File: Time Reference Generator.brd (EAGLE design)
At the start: 46.7 x 45.7 mm, 10 parts, among them IC1 4060N, IC2 4013N, X1 CRYSTAL_TINY

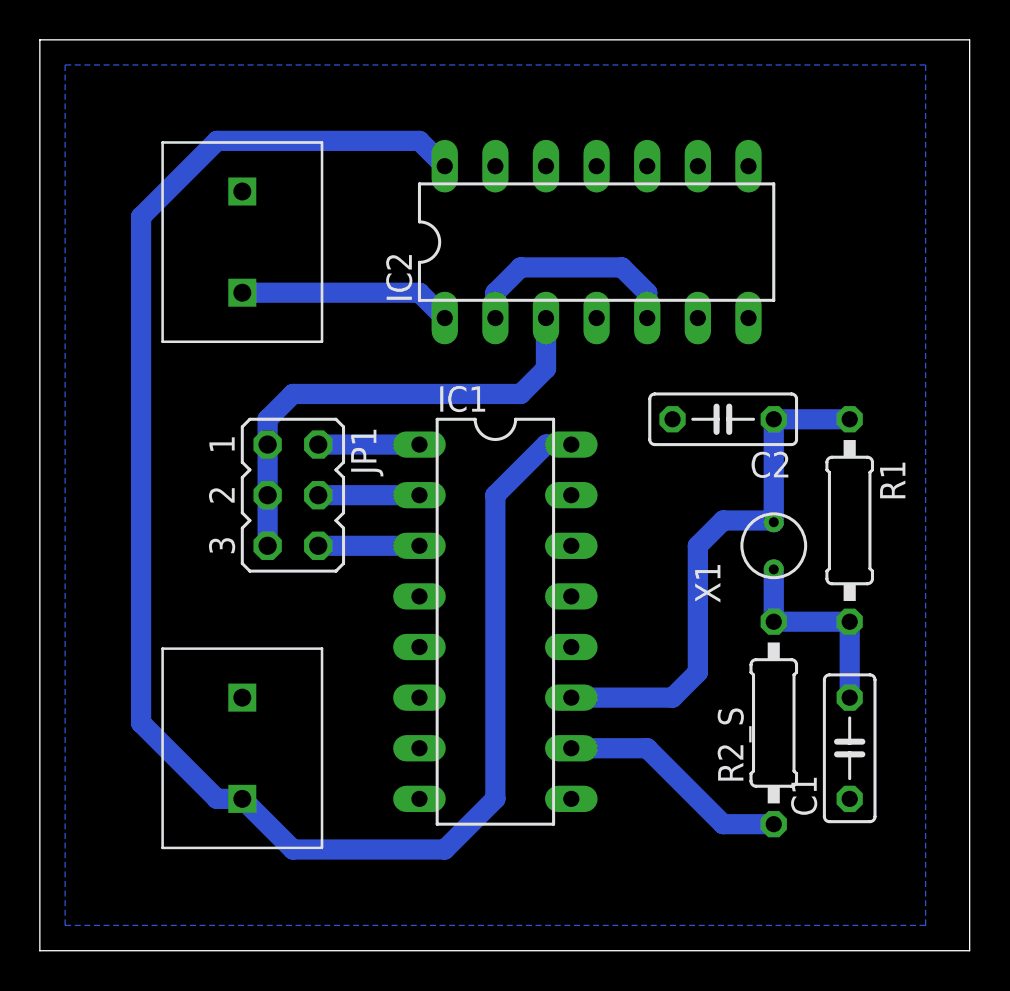
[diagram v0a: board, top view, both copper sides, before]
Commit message: Ajouter des capa de decouplage + augmentation isolation des thermals
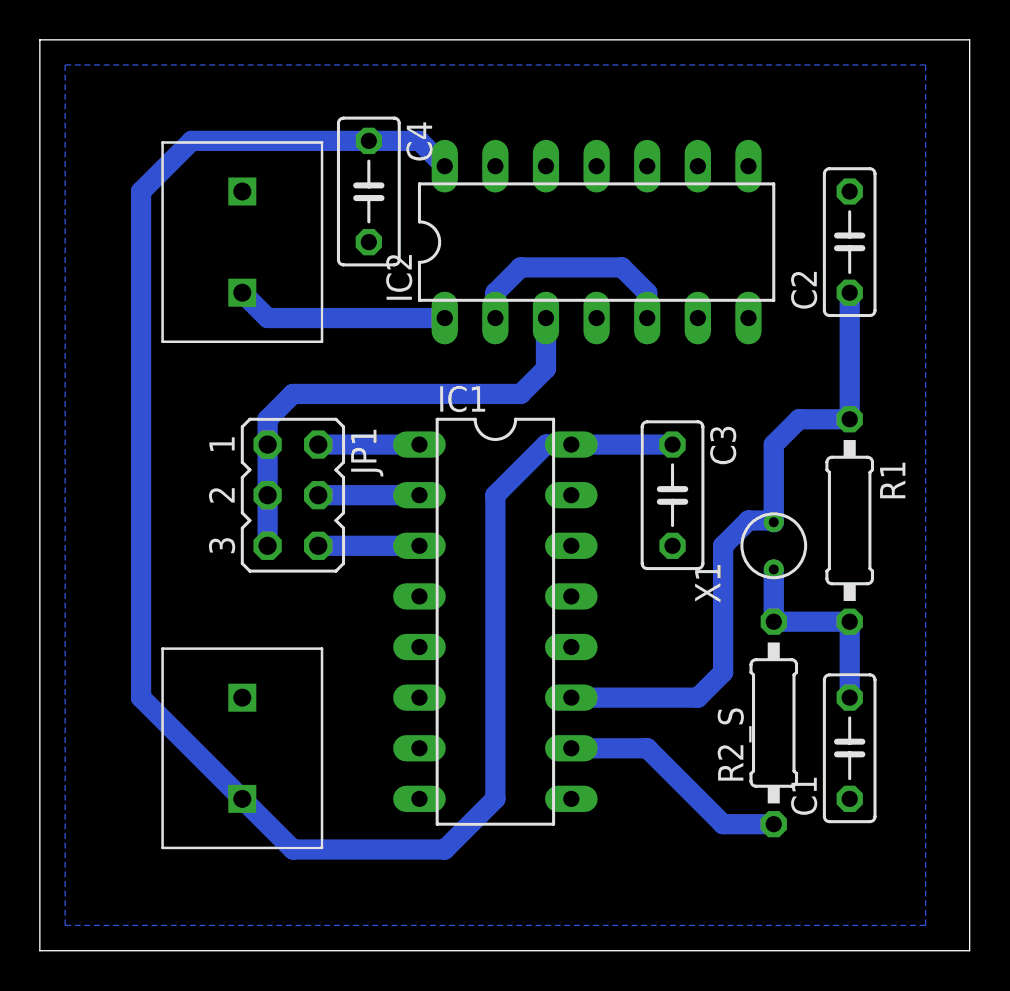
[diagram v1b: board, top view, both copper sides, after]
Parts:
- added C3, C4: 100n, resistor:C050-030X075
- moved C2 10.9 mm to (40.6, 35.6), turned to 90 degrees
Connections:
- net GND: now also C3.2, C4.2
- net VDD: now also C3.1, C4.1
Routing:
- net N$1: track 26.6 -> 32.2 mm
- net VDD: track 84.3 -> 89.4 mm
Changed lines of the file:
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@@
 <param name="srMinRoundness" value="0mil"/>
 <param name="srMaxRoundness" value="0mil"/>
-<param name="slThermalIsolate" value="10mil"/>
+<param name="slThermalIsolate" value="25mil"/>
 <param name="slThermalsForVias" value="0"/>
 <param name="dpMaxLengthDifference" value="10mm"/>
@@
 <element name="R1" library="resistor" package="0207/10" value="10M" x="40.64" y="21.59" rot="R270"/>
 <element name="C1" library="resistor" package="C050-025X075" value="25p" x="40.64" y="10.16" rot="R90"/>
-<element name="C2" library="resistor" package="C050-025X075" value="25p" x="34.29" y="26.67" rot="R180"/>
+<element name="C2" library="resistor" package="C050-025X075" value="25p" x="40.64" y="35.56" rot="R90"/>
 <element name="IC2" library="40xx" package="DIL14" value="4013N" x="27.94" y="35.56"/>
 <element name="POWER_SUPPY" library="PGT" package="SIL_2_0.2INCH" value="CON_2_SIL" x="10.16" y="10.16" rot="R180"/>
@@
 <element name="JP1" library="jumper" package="JP3Q" value="FREQ_SELECT" x="12.7" y="22.86" rot="R270"/>
 <element name="X1" library="PGT" package="WATCH-3X8-SPACED" value="CRYSTAL_TINY" x="36.83" y="20.32" rot="R90"/>
+<element name="C3" library="resistor" package="C050-030X075" value="100n" x="31.75" y="22.86" rot="R270"/>
+<element name="C4" library="resistor" package="C050-030X075" value="100n" x="16.51" y="38.1" rot="R270"/>
 </elements>
 <signals>
@@
 <wire x1="22.86" y1="22.86" x2="25.4" y2="25.4" width="1.016" layer="16"/>
 <wire x1="25.4" y1="25.4" x2="26.67" y2="25.4" width="1.016" layer="16"/>
-<wire x1="20.32" y1="39.37" x2="19.05" y2="40.64" width="1.016" layer="16"/>
-<wire x1="19.05" y1="40.64" x2="8.89" y2="40.64" width="1.016" layer="16"/>
-<wire x1="8.89" y1="40.64" x2="5.08" y2="36.83" width="1.016" layer="16"/>
-<wire x1="5.08" y1="36.83" x2="5.08" y2="11.43" width="1.016" layer="16"/>
-<wire x1="5.08" y1="11.43" x2="8.89" y2="7.62" width="1.016" layer="16"/>
-<wire x1="8.89" y1="7.62" x2="10.16" y2="7.62" width="1.016" layer="16"/>
+<contactref element="C3" pad="1"/>
+<contactref element="C4" pad="1"/>
+<wire x1="26.67" y1="25.4" x2="31.75" y2="25.4" width="1.016" layer="16"/>
+<wire x1="16.51" y1="40.64" x2="7.62" y2="40.64" width="1.016" layer="16"/>
+<wire x1="7.62" y1="40.64" x2="5.08" y2="38.1" width="1.016" layer="16"/>
+<wire x1="5.08" y1="38.1" x2="5.08" y2="12.7" width="1.016" layer="16"/>
+<wire x1="5.08" y1="12.7" x2="10.16" y2="7.62" width="1.016" layer="16"/>
+<wire x1="16.51" y1="40.64" x2="19.05" y2="40.64" width="1.016" layer="16"/>
+<wire x1="19.05" y1="40.64" x2="20.32" y2="39.37" width="1.016" layer="16"/>
 </signal>
 <signal name="GND">
@@
 <vertex x="44.45" y="44.45"/>
 </polygon>
+<contactref element="C3" pad="2"/>
+<contactref element="C4" pad="2"/>
 </signal>
 <signal name="8_HZ">
@@
 <contactref element="IC2" pad="1"/>
 <contactref element="OUTPUT" pad="P$1"/>
-<wire x1="10.16" y1="33.02" x2="19.05" y2="33.02" width="1.016" layer="16"/>
-<wire x1="19.05" y1="33.02" x2="20.32" y2="31.75" width="1.016" layer="16"/>
+<wire x1="20.32" y1="31.75" x2="11.43" y2="31.75" width="1.016" layer="16"/>
+<wire x1="11.43" y1="31.75" x2="10.16" y2="33.02" width="1.016" layer="16"/>
 </signal>
 <signal name="N$5">
@@
 <contactref element="C2" pad="1"/>
 <contactref element="R1" pad="1"/>
-<wire x1="36.83" y1="26.67" x2="40.64" y2="26.67" width="1.016" layer="16"/>
+<wire x1="40.64" y1="33.02" x2="40.64" y2="26.67" width="1.016" layer="16"/>
 <contactref element="IC1" pad="11"/>
 <contactref element="X1" pad="2"/>
-<wire x1="36.83" y1="26.67" x2="36.83" y2="21.505" width="1.016" layer="16"/>
 <wire x1="36.83" y1="21.505" x2="36.745" y2="21.59" width="1.016" layer="16"/>
-<wire x1="36.745" y1="21.59" x2="34.29" y2="21.59" width="1.016" layer="16"/>
-<wire x1="34.29" y1="21.59" x2="33.02" y2="20.32" width="1.016" layer="16"/>
-<wire x1="33.02" y1="20.32" x2="33.02" y2="13.97" width="1.016" layer="16"/>
-<wire x1="33.02" y1="13.97" x2="31.75" y2="12.7" width="1.016" layer="16"/>
-<wire x1="31.75" y1="12.7" x2="26.67" y2="12.7" width="1.016" layer="16"/>
+<wire x1="36.745" y1="21.59" x2="35.56" y2="21.59" width="1.016" layer="16"/>
+<wire x1="35.56" y1="21.59" x2="34.29" y2="20.32" width="1.016" layer="16"/>
+<wire x1="34.29" y1="20.32" x2="34.29" y2="13.97" width="1.016" layer="16"/>
+<wire x1="34.29" y1="13.97" x2="33.02" y2="12.7" width="1.016" layer="16"/>
+<wire x1="33.02" y1="12.7" x2="26.67" y2="12.7" width="1.016" layer="16"/>
+<wire x1="40.64" y1="26.67" x2="38.1" y2="26.67" width="1.016" layer="16"/>
+<wire x1="38.1" y1="26.67" x2="36.83" y2="25.4" width="1.016" layer="16"/>
+<wire x1="36.83" y1="25.4" x2="36.83" y2="21.505" width="1.016" layer="16"/>
 </signal>
 <signal name="N$3">
